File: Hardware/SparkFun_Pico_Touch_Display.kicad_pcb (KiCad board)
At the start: 4 copper layers, 58.4 x 50.8 mm, 73 parts, among them J1 Conn_01x20, J2 Conn_01x20, J3 Conn_02x10_SMD_RA, J4 Conn_1x21_FPC, J5 Qwiic_Vertical, J6 microSD, Q1 RE1C002UNTCL, SW1 SMD_4.6x2.8mm_h2.5mm, U1 2" LCD-TFT 240x320

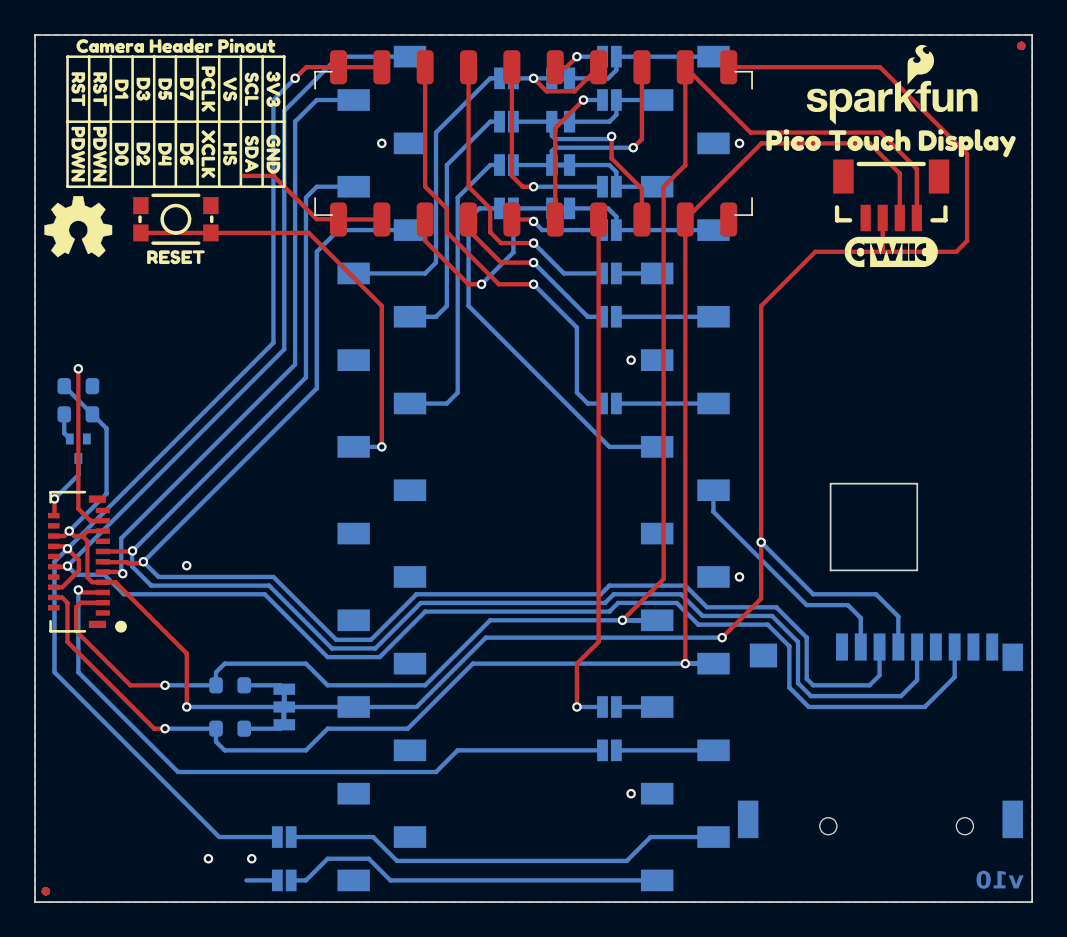
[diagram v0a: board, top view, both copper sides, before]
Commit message: Clean up design
Finish routing
Add power LED
Move all schematic elements inside frame
Update display 3D model
Stitch together GND pours
Add measures
Fill out sheet info
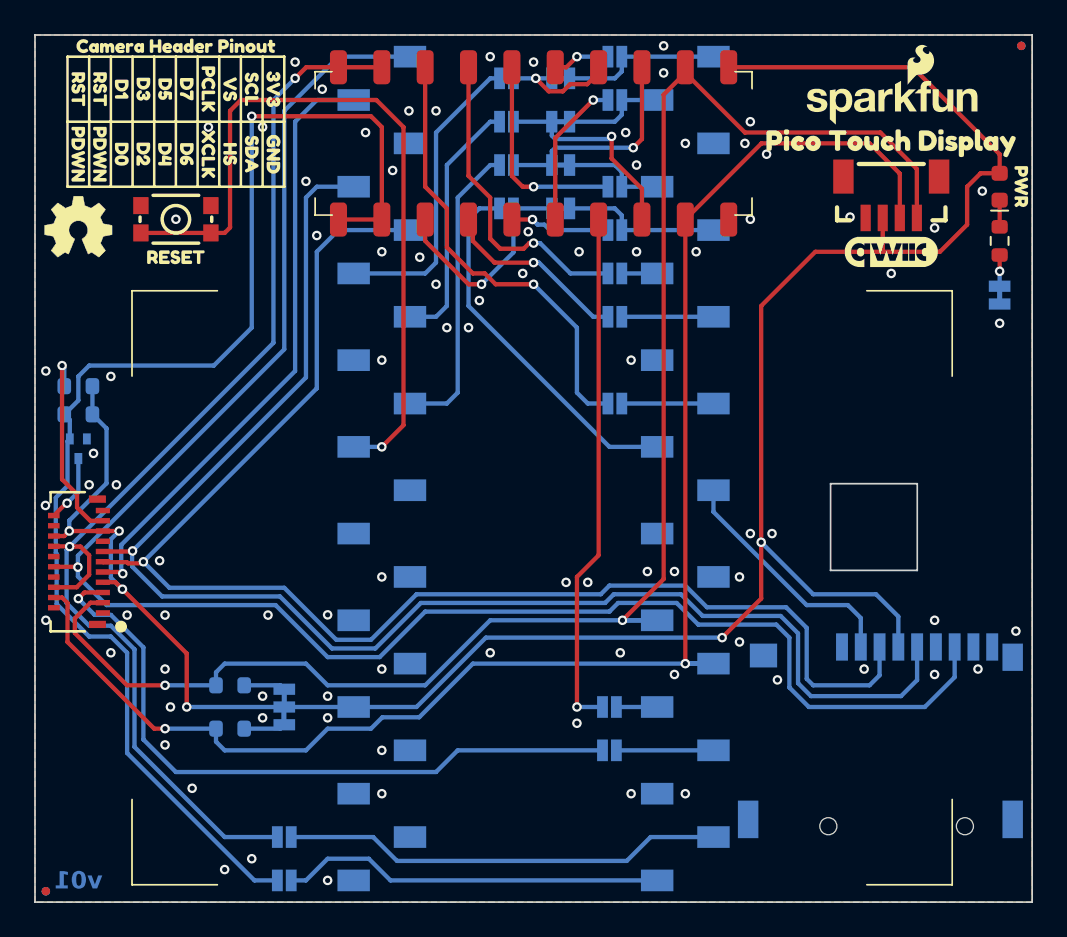
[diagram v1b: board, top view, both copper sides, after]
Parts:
- added D1: Red, SparkFun-LED:LED_0603_1608Metric_Red, F.Cu at (172.1, 82.5)
- added JP21: ~, SparkFun-Jumper:Jumper_2_NC_Trace, B.Cu at (172.1, 88.9)
- added R5: 4.7k, SparkFun-Resistor:R_0603_1608Metric, F.Cu at (172.1, 85.7)
- added kibuzzard-67B3EC79: G***, kibuzzard-67B3EC79, B.Cu at (165.7, 80.0)
- added kibuzzard-67C1248C: G***, kibuzzard-67C1248C, F.Cu at (173.4, 82.5)
- added kibuzzard-67C124A5: G***, kibuzzard-67C124A5, B.Cu at (170.5, 88.9)
- moved kibuzzard-67B3FF8F 0.44 mm to (128.0, 123.2)
- moved JP10 0.32 mm to (149.5, 82.5)
- moved JP11 0.32 mm to (149.5, 77.5)
- moved JP12 0.32 mm to (149.5, 74.9)
- moved JP6 0.32 mm to (149.5, 87.6)
- moved JP7 0.32 mm to (149.5, 90.2)
- moved JP8 0.32 mm to (149.5, 95.2)
- moved JP9 0.32 mm to (149.5, 85.1)
- moved kibuzzard-67B3FF95 0.32 mm to (145.7, 115.6)
- turned R1 to 0 degrees
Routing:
- net CAM_PWDN: track 12.7 -> 76.8 mm, vias 0 -> 1
- net RUN: track 25.8 -> 44.2 mm
- net 3.3V: track 128.3 -> 131.4 mm, vias 4 -> 6
- net Net-(J4-Pin_3): track 9.93 -> 11.8 mm
- net Net-(JP21-A): track 0.00 -> 1.83 mm, vias 0 -> 1
- net Net-(D1-K): track 0.00 -> 1.56 mm
- net CAM_~{RST}: track 67.3 -> 68.8 mm
- net CAM_D1: track 25.7 -> 26.5 mm
- net CAM_D3: track 17.8 -> 18.6 mm
- net CAM_D2: track 10.6 -> 11.1 mm
- net GND: vias 8 -> 88
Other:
- board text added: "v01"
- board text removed: "v10"

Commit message: Design review updates
Rename jumpers to match silk
Nudge traces to provide more isolation of I2C traces
Add 10uF capacitor for uSD card
Fix acid trap
Rename MISO/MOSI to POCI/PICO
Increase 3.3V trace width
Change to 2 layer
Update ordering notes
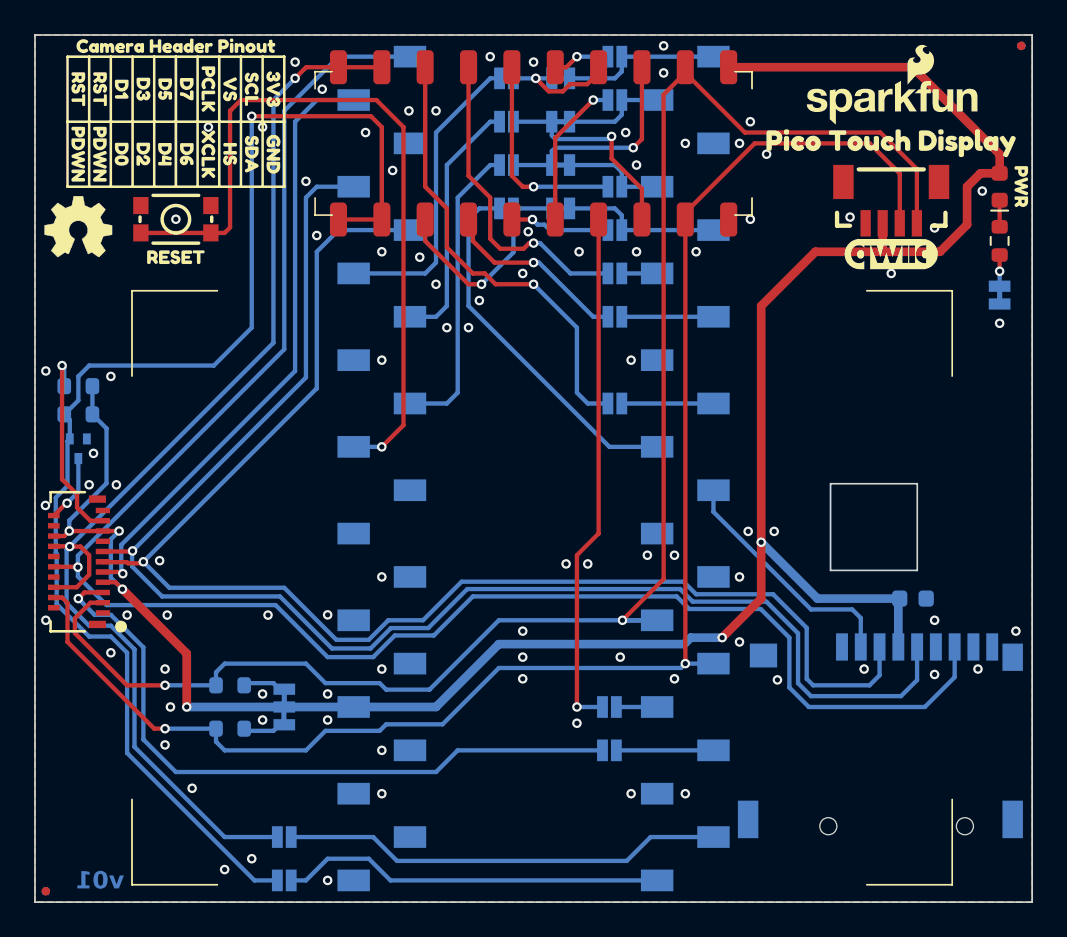
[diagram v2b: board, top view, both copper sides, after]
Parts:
- added C1: 10uF, SparkFun-Capacitor:C_0603_1608Metric, B.Cu at (167.0, 106.7)
- JP1: value ~ -> I2C
- JP10: value ~ -> 8-BIT-D5
- JP11: value ~ -> 8-BIT-D6
- JP12: value ~ -> 8-BIT-D7
- JP13: value ~ -> MCLK
- JP14: value ~ -> ~{RST}
- JP15: value ~ -> TP_INT
- JP16: value ~ -> LP
- JP17: value ~ -> 1-BIT-PCLK
- JP18: value ~ -> 1-BIT-HS
- JP19: value ~ -> 1-BIT-VS
- JP2: value ~ -> 8-BIT-D0
- JP20: value ~ -> 1-BIT-D0
- JP21: value ~ -> PWR
- JP3: value ~ -> 8-BIT-VS
- JP4: value ~ -> 8-BIT-HS
- JP5: value ~ -> 8-BIT-PCLK
- JP6: value ~ -> 8-BIT-D3
- JP7: value ~ -> 8-BIT-D2
- JP8: value ~ -> 8-BIT-D1
- JP9: value ~ -> 8-BIT-D4
- moved J5 0.32 mm to (165.7, 83.2)
- moved G*** 0.13 mm to (165.7, 86.5)
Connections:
- net DISP_MOSI renamed DISP_PICO
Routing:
- net CAM_SDA: track 91.7 -> 90.6 mm
- net CAM_SCL: track 96.1 -> 96.6 mm
- net GND: vias 88 -> 90
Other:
- copper layers 4 -> 2
- board text added: "Finish: Lead-Free HASL"
- board text added: "Layers: 2"
- board text added: "Material: TG135"
- board text removed: "Controlled Impedance: JLC04161H-7628"
- board text removed: "Finish: ENIG"
- board text removed: "Inner Copper Weight: 0.5oz"
- board text removed: "Layers: 4"
- board text removed: "Material: TG155"
- board text removed: "No Clean Process"

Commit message: Design review updates
Change to 4 layer
Add GPIO expander for control signals
Connect uSD detection pin
Fix typo in company name on schematic
Update datahseet link for 21-pin FPC connector
Update KiCad libraries
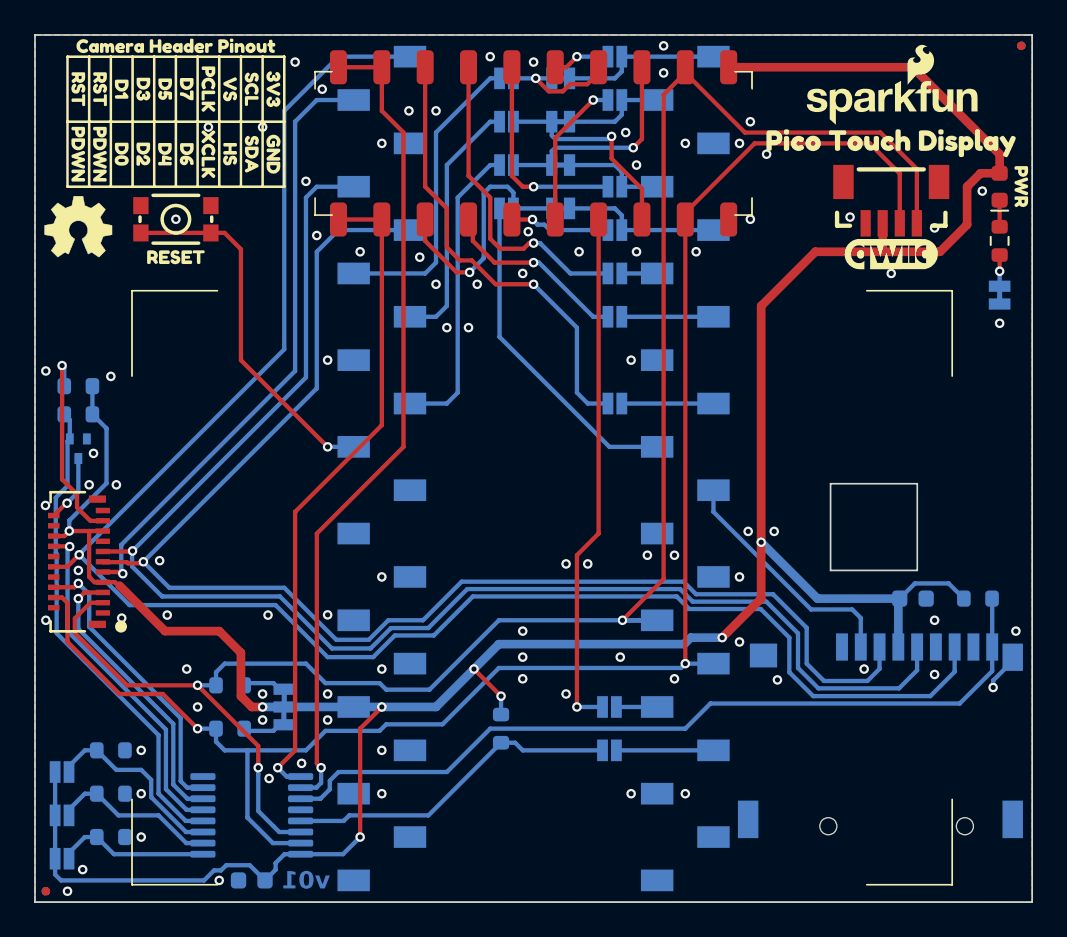
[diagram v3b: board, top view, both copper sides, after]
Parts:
- removed kibuzzard-67B3FF8F: G***, kibuzzard-67B3FF8F
- removed kibuzzard-67B3FF95: G***, kibuzzard-67B3FF95
- removed kibuzzard-67B3FFB7: G***, kibuzzard-67B3FFB7
- added C2: 0.1uF, SparkFun-Capacitor:C_0603_1608Metric, B.Cu at (128.3, 123.2)
- added JP22: ~{INT}, SparkFun-Jumper:Jumper_2_NO, B.Cu at (149.2, 115.6)
- added R10: 100k, SparkFun-Resistor:R_0603_1608Metric, B.Cu at (170.8, 106.7)
- added R6: 100k, SparkFun-Resistor:R_0603_1608Metric, B.Cu at (142.9, 114.3)
- added R7: 100k, SparkFun-Resistor:R_0603_1608Metric, B.Cu at (120.0, 120.7)
- added R8: 100k, SparkFun-Resistor:R_0603_1608Metric, B.Cu at (120.0, 118.1)
- added R9: 100k, SparkFun-Resistor:R_0603_1608Metric, B.Cu at (120.0, 115.6)
- added U2: PCA9554PW, SparkFun-Semiconductor-Standard:TSSOP-16_4.4x5mm_P0.65mm, B.Cu at (128.3, 119.4)
- added kibuzzard-67C64429: G***, kibuzzard-67C64429, B.Cu at (119.5, 121.9)
- added kibuzzard-67C6452E: G***, kibuzzard-67C6452E, B.Cu at (119.5, 116.8)
- added kibuzzard-67C64532: G***, kibuzzard-67C64532, B.Cu at (119.4, 119.4)
- added kibuzzard-67C651AF: G***, kibuzzard-67C651AF, B.Cu at (146.7, 115.6)
- JP14: value ~{RST} -> A0
- JP15: value TP_INT -> A1
- JP16: value LP -> A2
- moved JP15 32.3 mm to (117.2, 119.4), turned to 180 degrees
- moved JP16 14.5 mm to (117.2, 116.8), turned to 180 degrees
- moved JP14 13.1 mm to (117.2, 121.9), turned to 180 degrees
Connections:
- net CAM_SCL renamed SCL/GPIO5
- net CAM_SDA renamed SDA/GPIO4
- net DISP_CLK renamed GPIO18/SCK
- net DISP_DC renamed GPIO16/POCI/DC
- net DISP_PICO renamed GPIO19/PICO
- net DISP_~{CS} renamed GPIO17/DISP_~{CS}
- net GPIO7 renamed GPIO7/SD_~{CS}
- J1 pad 1: GPIO0 -> unconnected-(J1-Pin_1-Pad1)
- J1 pad 2: GPIO1 -> unconnected-(J1-Pin_2-Pad2)
- J1 pad 9: GPIO6 -> unconnected-(J1-Pin_9-Pad9)
- J2 pad 1: VBUS -> unconnected-(J2-Pin_1-Pad1)
- J2 pad 10: GPIO26 -> unconnected-(J2-Pin_10-Pad10)
- J2 pad 2: VSYS -> unconnected-(J2-Pin_2-Pad2)
- J2 pad 4: 3V3_EN -> unconnected-(J2-Pin_4-Pad4)
- J2 pad 6: ADC_VREF -> unconnected-(J2-Pin_6-Pad6)
- J2 pad 7: GPIO28 -> unconnected-(J2-Pin_7-Pad7)
- J2 pad 9: GPIO27 -> unconnected-(J2-Pin_9-Pad9)
- J4 pad 16: CAM_~{RST} -> TP_~{RESET}
- J4 pad 8: CAM_~{RST} -> DISP_~{RST}
- J6 pad 9: unconnected-(J6-~{DET}-Pad9) -> SD_DET
- JP14 pad 1: CAM_~{RST} -> A0
- JP14 pad 2: GPIO1 -> 3.3V
- JP15 pad 1: TP_INT -> A1
- JP15 pad 2: GPIO2 -> 3.3V
- JP16 pad 1: CAM_PWDN -> A2
- JP16 pad 2: GPIO0 -> 3.3V
- Q1 pad 1: CAM_PWDN -> DISP_BL
- R2 pad 1: CAM_PWDN -> DISP_BL
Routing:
- net SD_DET: track 0.00 -> 48.2 mm
- net 3.3V: track 131.9 -> 172.3 mm, vias 6 -> 8
- net CAM_PWDN: track 76.8 -> 38.7 mm
- net DISP_BL: track 0.00 -> 28.5 mm
- net GPIO1: track 25.9 -> 0.00 mm
- net TP_INT: track 40.2 -> 16.9 mm
- net RUN: track 44.2 -> 21.5 mm
- net GPIO0: track 22.5 -> 0.00 mm
- net CAM_~{RST}: track 68.8 -> 48.5 mm, vias 2 -> 1
- net DISP_~{RST}: track 0.00 -> 20.3 mm, vias 0 -> 1
- net ~{INT}: track 0.00 -> 19.8 mm
- net TP_~{RESET}: track 0.00 -> 17.1 mm, vias 0 -> 1
- net SCL/GPIO5: track 96.6 -> 108.4 mm, vias 2 -> 3
- net A2: track 0.00 -> 11.1 mm
- net A1: track 0.00 -> 9.77 mm
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- added copper zone on In1.Cu, net GND
- added copper zone on In2.Cu, net GND
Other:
- copper layers 2 -> 4
- board text added: "Inner Copper Weight: 0.5oz"
- board text added: "Layers: 4"
- board text removed: "Layers: 2"

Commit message: Design review updates
Fix NC flags on headers and GPIO expander
Change In2.Cu to 3.3V instead of GND
Fix MOSFET datasheet link
Move Qwiic silk
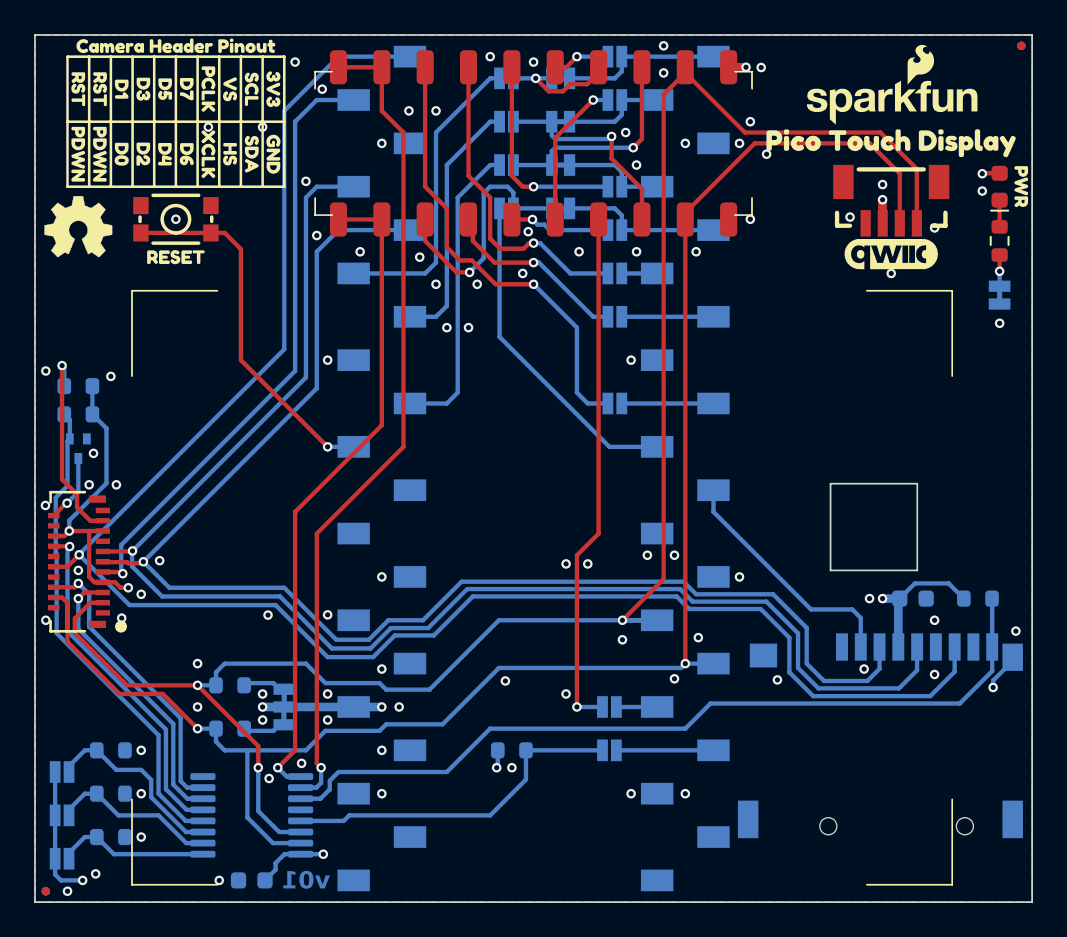
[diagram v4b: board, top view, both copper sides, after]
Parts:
- moved R6 1.42 mm to (143.5, 115.6), turned to 180 degrees
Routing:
- net 3.3V: track 172.3 -> 49.2 mm, vias 8 -> 11
- net ~{INT}: track 19.8 -> 20.4 mm
- net GND: vias 92 -> 93
- added copper zone on In2.Cu, net 3.3V
- removed copper zone on In2.Cu, net GND

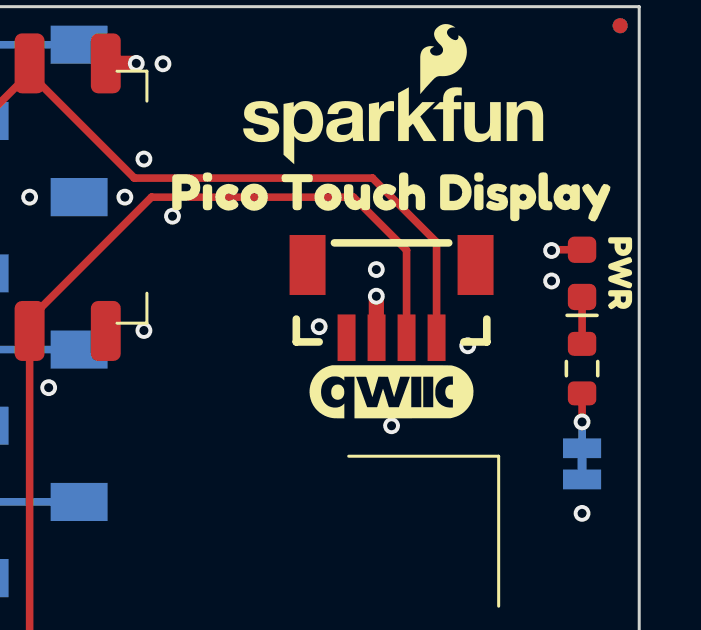
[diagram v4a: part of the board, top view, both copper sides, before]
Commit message: Actually save board file
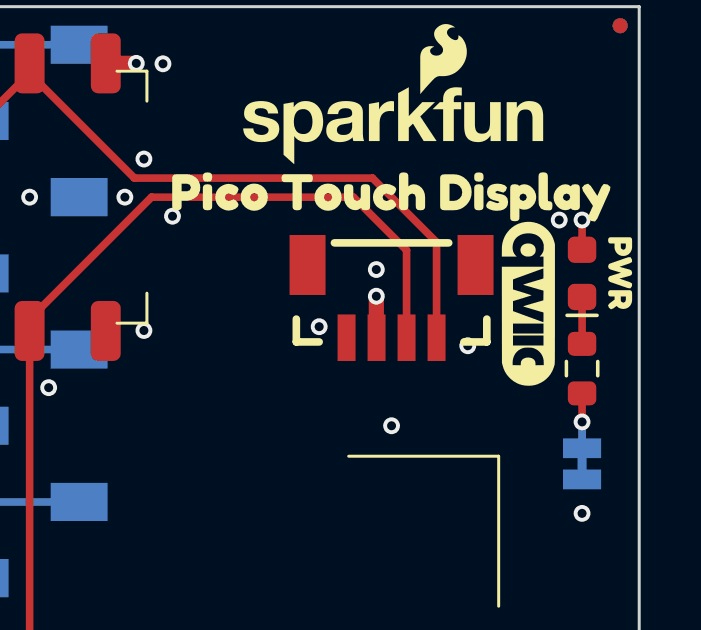
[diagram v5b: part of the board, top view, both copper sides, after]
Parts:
- moved G*** 5.43 mm to (170.3, 83.6), turned to -90 degrees
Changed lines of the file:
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@@
 	(footprint "SparkFun-Aesthetic:qwiic_5.5mm"
 		(layer "F.Cu")
-		(at 165.735 86.487)
+		(at 170.307 83.566 -90)
 		(tags "SparkFun")
 		(property "Reference" "G***"
-			(at 0 -1.3 0)
+			(at 0 -1.3 90)
 			(layer "F.Fab")
 			(hide yes)
@@
 		)
 		(property "Value" "LOGO"
-			(at 0 1.4 0)
+			(at 0 1.4 90)
 			(layer "F.Fab")
 			(hide yes)
@@
 		)
 		(property "Footprint" "SparkFun-Aesthetic:qwiic_5.5mm"
-			(at 0 0 0)
+			(at 0 0 -90)
 			(unlocked yes)
 			(layer "F.Fab")
@@
 		)
 		(property "Datasheet" ""
-			(at 0 0 0)
+			(at 0 0 -90)
 			(unlocked yes)
 			(layer "F.Fab")
@@
 		)
 		(property "Description" ""
-			(at 0 0 0)
+			(at 0 0 -90)
 			(unlocked yes)
 			(layer "F.Fab")
@@
 	)
 	(segment
-		(start 171.0945 81.7625)
-		(end 171.069 81.788)
-		(width 0.254)
-		(layer "F.Cu")
-		(net 2)
-	)
-	(segment
 		(start 119.056 105.721)
 		(end 118.745 105.41)
@@
 	)
 	(segment
-		(start 118.745 102.721001)
-		(end 117.580001 102.721001)
+		(start 172.085 80.772)
+		(end 172.085 81.7625)
 		(width 0.254)
 		(layer "F.Cu")
@@
 	)
 	(segment
-		(start 121.03789 106.045)
-		(end 120.58 106.045)
+		(start 118.745 102.721001)
+		(end 117.580001 102.721001)
 		(width 0.254)
 		(layer "F.Cu")
@@
 	)
 	(segment
-		(start 172.085 81.7625)
-		(end 171.0945 81.7625)
+		(start 121.03789 106.045)
+		(end 120.58 106.045)
 		(width 0.254)
 		(layer "F.Cu")
@@
 	)
 	(via
-		(at 171.069 81.788)
+		(at 172.085 80.772)
 		(size 0.56)
 		(drill 0.3)
@@
 	)
 	(via
-		(at 171.069 82.804)
+		(at 171.323 80.772)
 		(size 0.56)
 		(drill 0.3)
